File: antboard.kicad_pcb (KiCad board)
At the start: 2 copper layers, 6 parts, among them U4 OLED_0.96

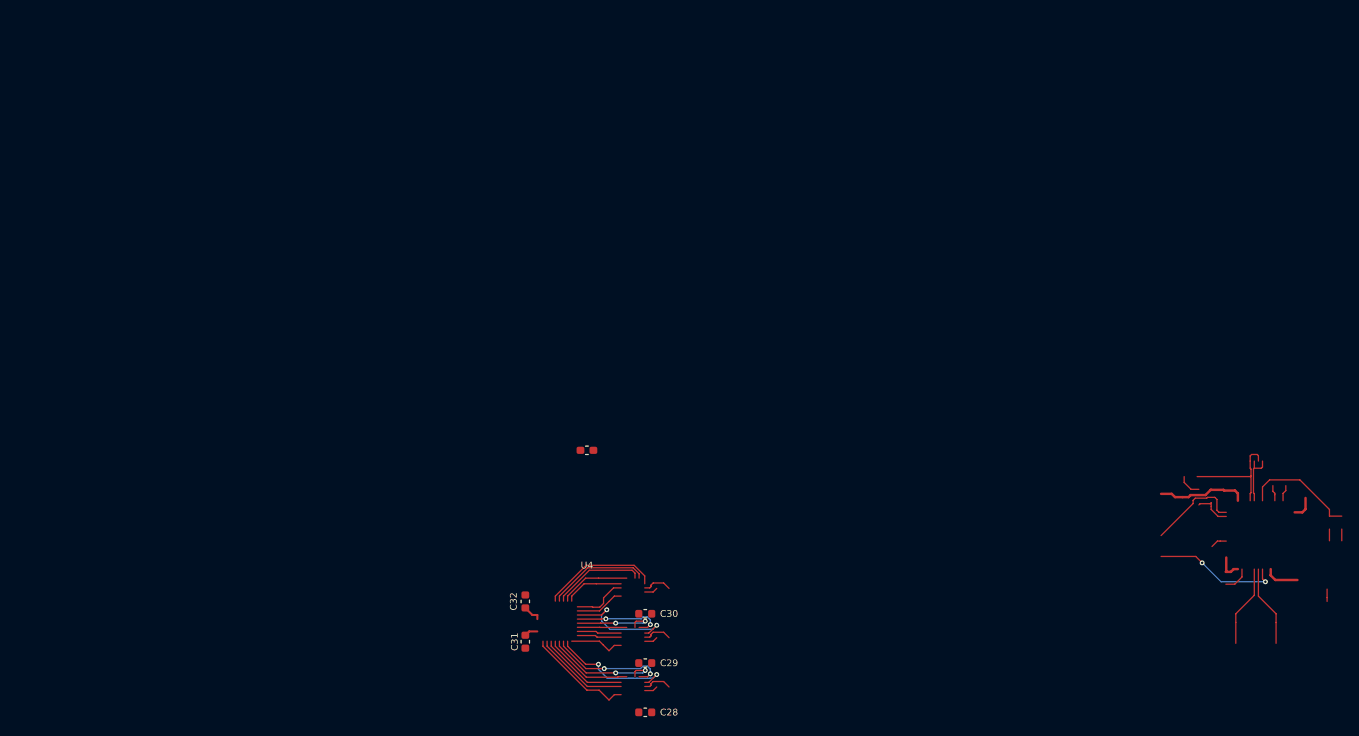
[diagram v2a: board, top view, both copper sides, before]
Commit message: Routing should be done
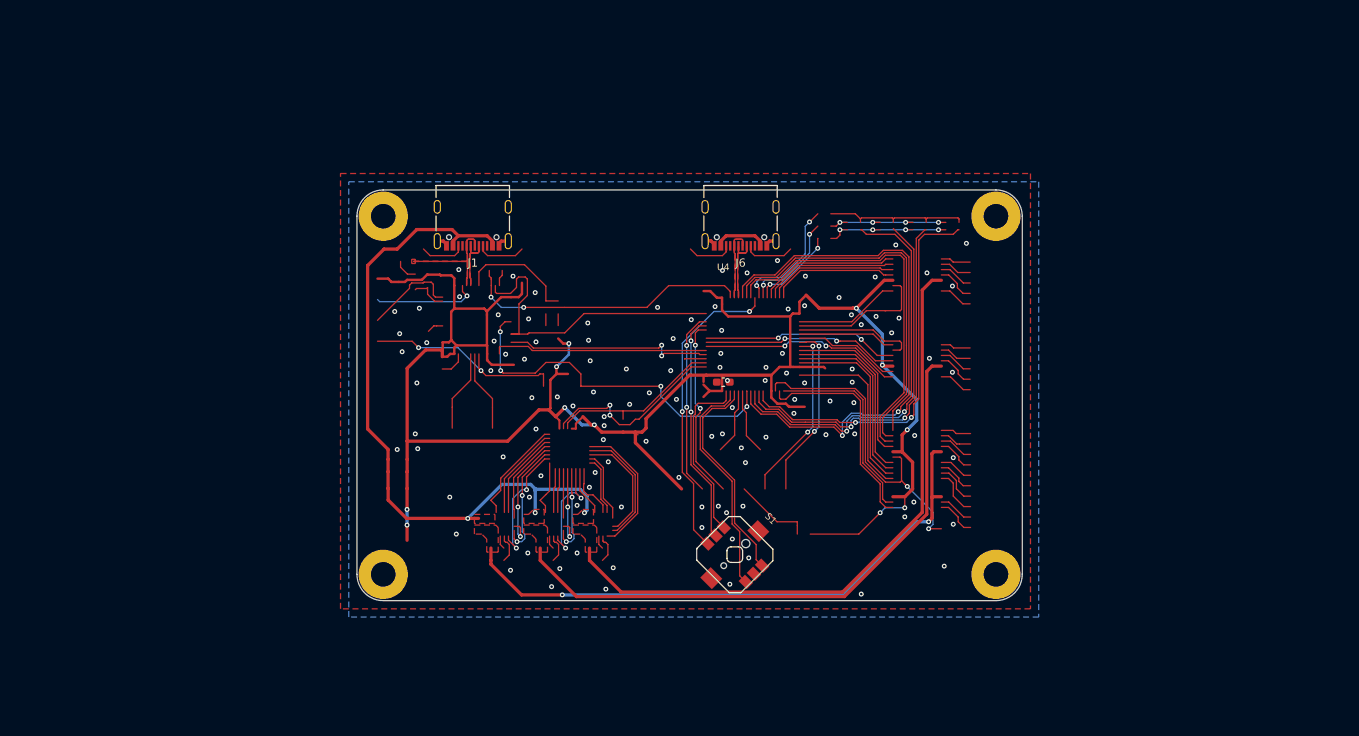
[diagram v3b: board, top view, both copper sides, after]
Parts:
- removed C28, C29, C30: 10u, Capacitor_SMD:C_0603_1608Metric
- removed C31, C32: 100n, Capacitor_SMD:C_0603_1608Metric
- added J1: USB_C_Receptacle_USB2.0, antboard:USB_C_Receptacle_Palconn_UTC16-G, F.Cu at (124.1, 75.3)
- added J6: USB_C_Receptacle_USB2.0, antboard:USB_C_Receptacle_Palconn_UTC16-G, F.Cu at (156.7, 75.3)
- added REF**: MountingHole_3mm_Pad, MountingHole:MountingHole_3mm_Pad, F.Cu at (113.2, 74.2)
- added REF**: MountingHole_3mm_Pad, MountingHole:MountingHole_3mm_Pad, F.Cu at (113.2, 117.8)
- added REF**: MountingHole_3mm_Pad, MountingHole:MountingHole_3mm_Pad, F.Cu at (187.8, 74.2)
- added REF**: MountingHole_3mm_Pad, MountingHole:MountingHole_3mm_Pad, F.Cu at (187.8, 117.8)
- added S1: K1-5202UA-03, antboard:K1-5202UA-03, F.Cu at (156.0, 115.4)
- moved U4 18.6 mm to (154.6, 94.4), turned to 180 degrees
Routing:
- net +3V3: track 25.4 -> 255.9 mm, vias 0 -> 11
- net +5V: track 0.00 -> 89.6 mm, vias 0 -> 3
- net PCVCC: track 0.00 -> 77.5 mm
- net PBVCC: track 0.00 -> 74.0 mm
- net PAVCC: track 0.00 -> 71.4 mm, vias 0 -> 2
- net /stm32/LED_A0: track 0.00 -> 51.0 mm, vias 0 -> 2
- net /stm32/LED_A3: track 0.00 -> 48.0 mm, vias 0 -> 2
- net /stm32/LED_A1: track 0.00 -> 46.8 mm, vias 0 -> 2
- net /io/PA8: track 0.00 -> 46.7 mm
- net /io/PA7: track 0.00 -> 46.5 mm
- net /io/PA9: track 0.00 -> 45.7 mm
- net /stm32/LED_A2: track 0.00 -> 45.5 mm, vias 0 -> 2
- net /st_link/SWRST: track 0.00 -> 44.3 mm, vias 0 -> 4
- net /st_link/SWCLK: track 0.00 -> 39.2 mm
- net /io/PAOE: track 0.00 -> 38.9 mm, vias 0 -> 2
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- added copper zone on F.Cu, net +5V
- added copper zone on F.Cu, net /st_link/USB_N
- added copper zone on F.Cu, net /st_link/USB_P
- added copper zone on F.Cu, net /stm32/USB_N
- added copper zone on F.Cu, net /stm32/USB_P
- added copper zone on B.Cu, net GND
- added copper zone on F.Cu, net GND
- added copper zone on F.Cu, net PAVCC
- added copper zone on F.Cu, net PBVCC
- added copper zone on F.Cu, net PCVCC
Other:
- board outline added: 81 x 50 mm

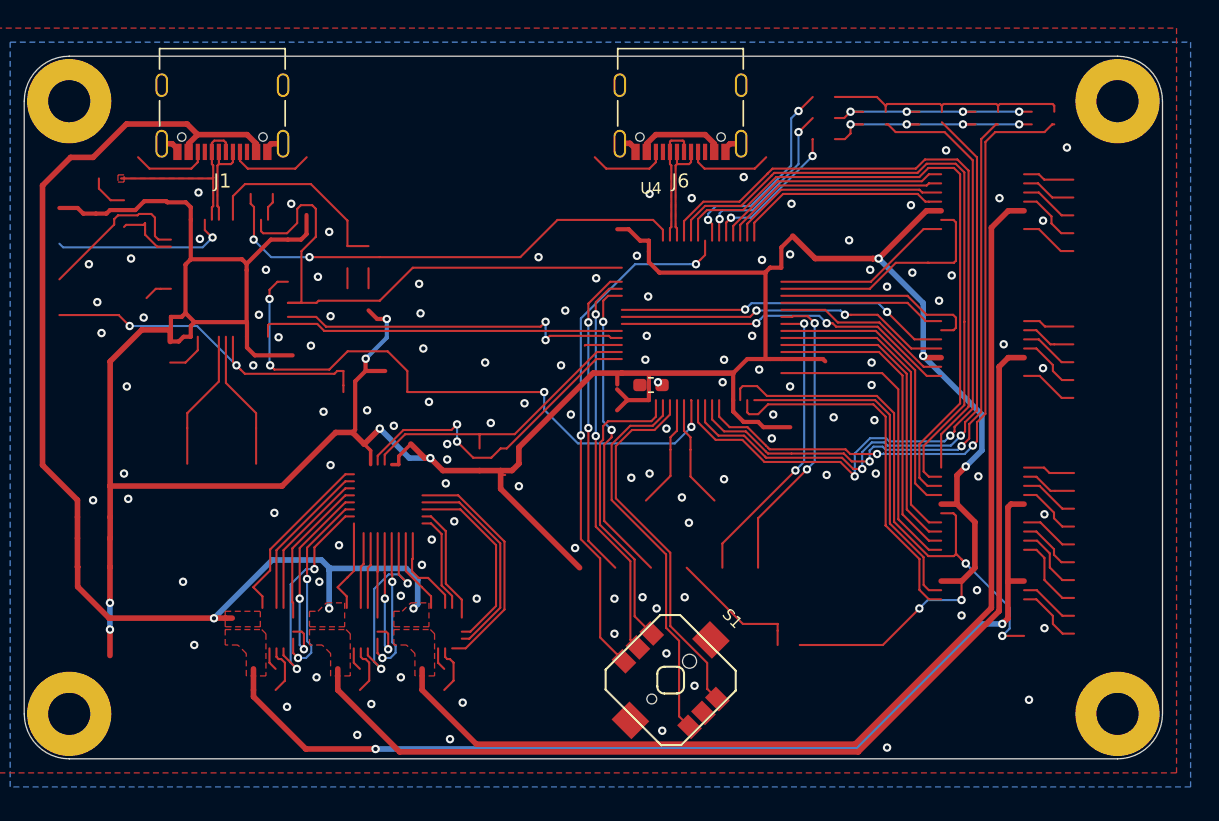
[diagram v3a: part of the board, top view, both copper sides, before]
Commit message: Stitch ground and add ants to silkscreen
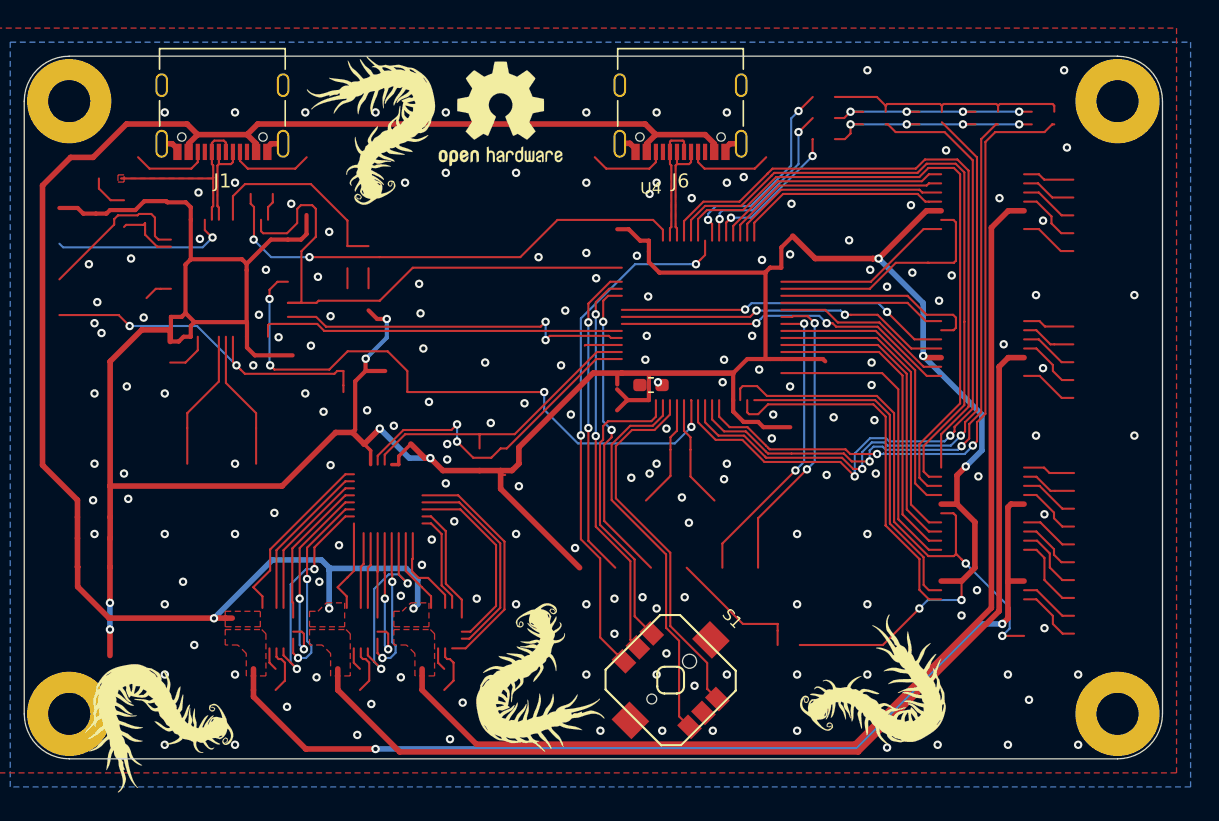
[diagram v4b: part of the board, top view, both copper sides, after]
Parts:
- added G***: LOGO, antboard:ant, F.Cu at (170.4, 115.5)
- added G***: LOGO, antboard:ant, F.Cu at (119.4, 119.3)
- added G***: LOGO, antboard:ant, F.Cu at (147.2, 115.4)
- added G***: LOGO, antboard:ant, F.Cu at (134.2, 76.1)
- added REF**: OSHW-Logo2_9.8x8mm_SilkScreen, Symbol:OSHW-Logo2_9.8x8mm_SilkScreen, F.Cu at (143.9, 75.1)
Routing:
- net +5V: track 89.6 -> 119.3 mm
- net GND: vias 115 -> 175
